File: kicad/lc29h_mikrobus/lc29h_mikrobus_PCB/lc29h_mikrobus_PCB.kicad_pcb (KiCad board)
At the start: 2 copper layers, 27.4 x 57.5 mm, 47 parts, among them IC1 MIKROE-924, IC101 DS28E36BQ+U, IC102 74LVC1G3157GV,125, J1 Conn_Coaxial, J2 Conn_01x03_Pin, Q1 DMP3013SFV, Q101 BC856B-13-F, Q102 BSS123L, Q3 BSS123L, Q4 PN2222A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

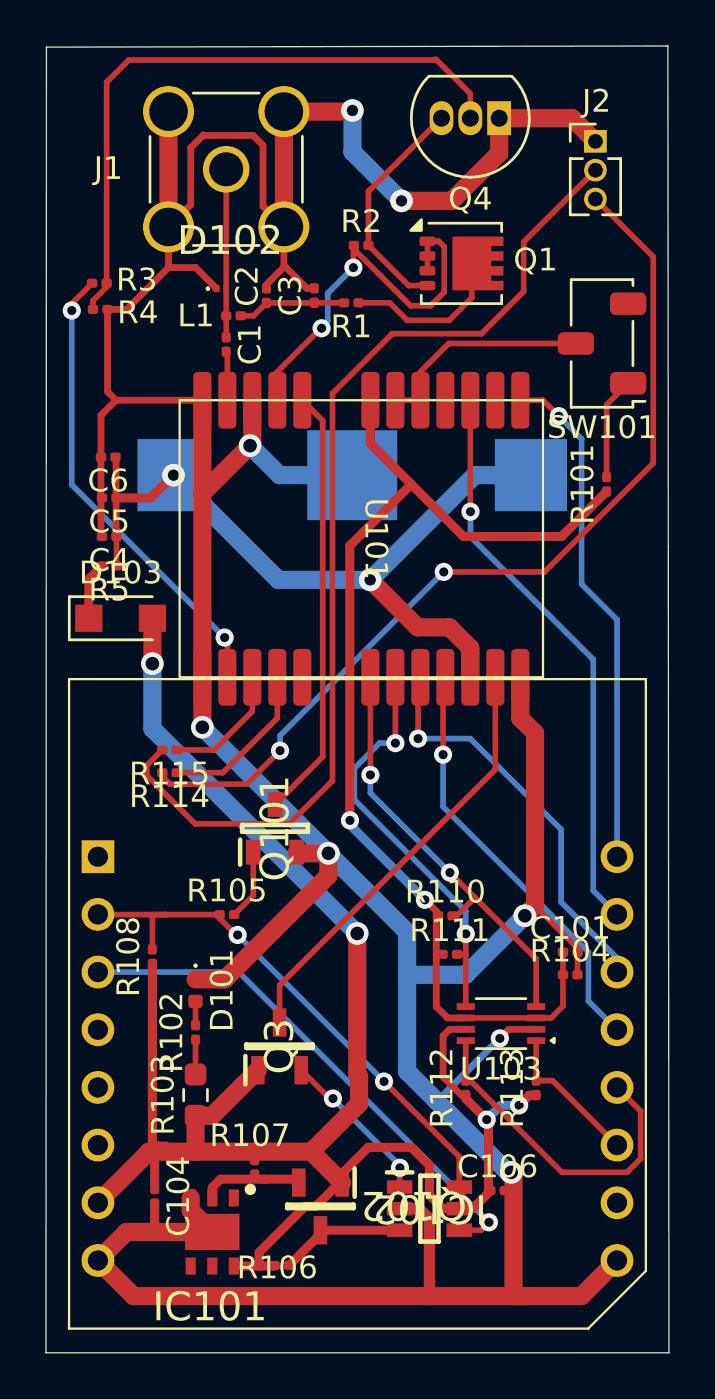
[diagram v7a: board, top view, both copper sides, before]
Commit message: replace explicit ground routing with ground plane
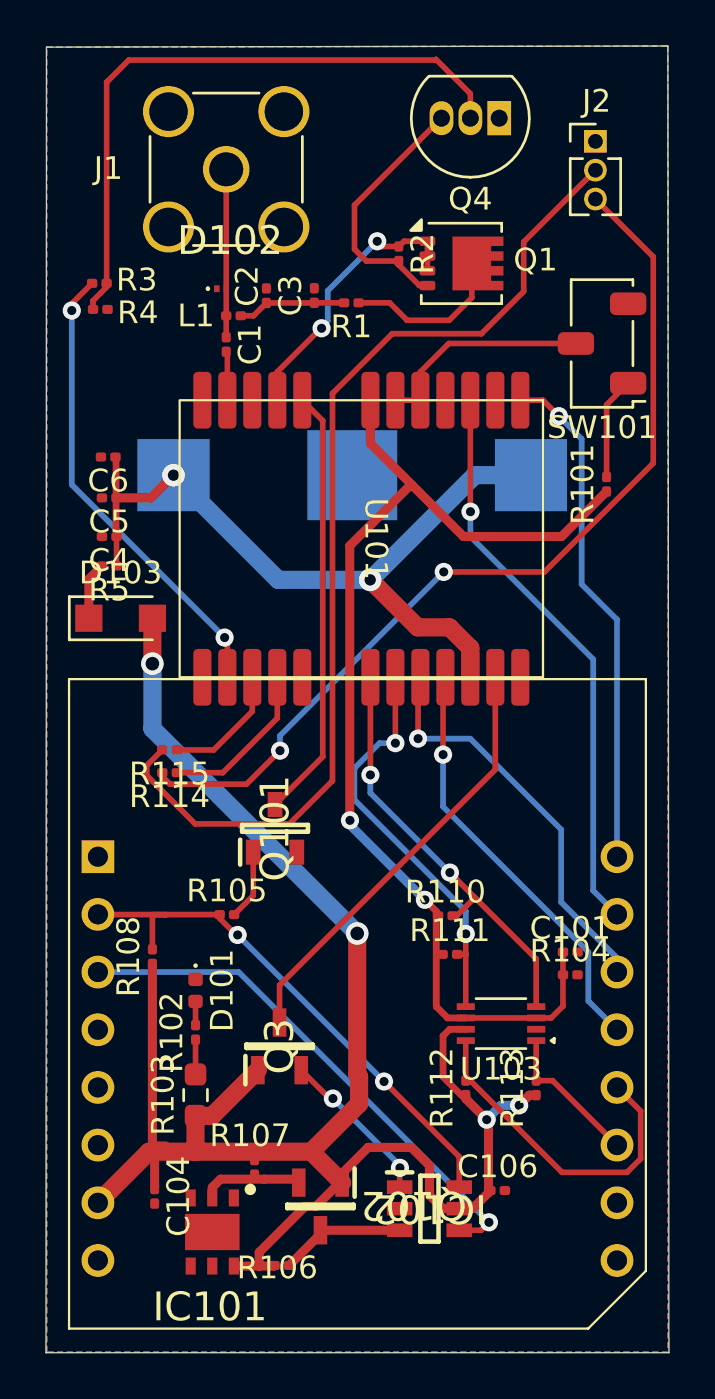
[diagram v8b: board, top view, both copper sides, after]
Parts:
- moved R2 1.70 mm to (139.3, 48.7), turned to -90 degrees
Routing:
- net GND: track 197.3 -> 0.00 mm, vias 8 -> 0
- net VDD_RF: track 17.8 -> 12.5 mm
- net Net-(Q1-G): track 10.3 -> 11.3 mm
- added copper zone on B.Cu, net GND
- added copper zone on F.Cu, net GND
